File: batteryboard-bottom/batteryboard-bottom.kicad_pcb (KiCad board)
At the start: 2 copper layers, 46.8 x 46.8 mm, 7 parts, among them J1 Conn_01x10, J2 Conn_02x05_Odd_Even

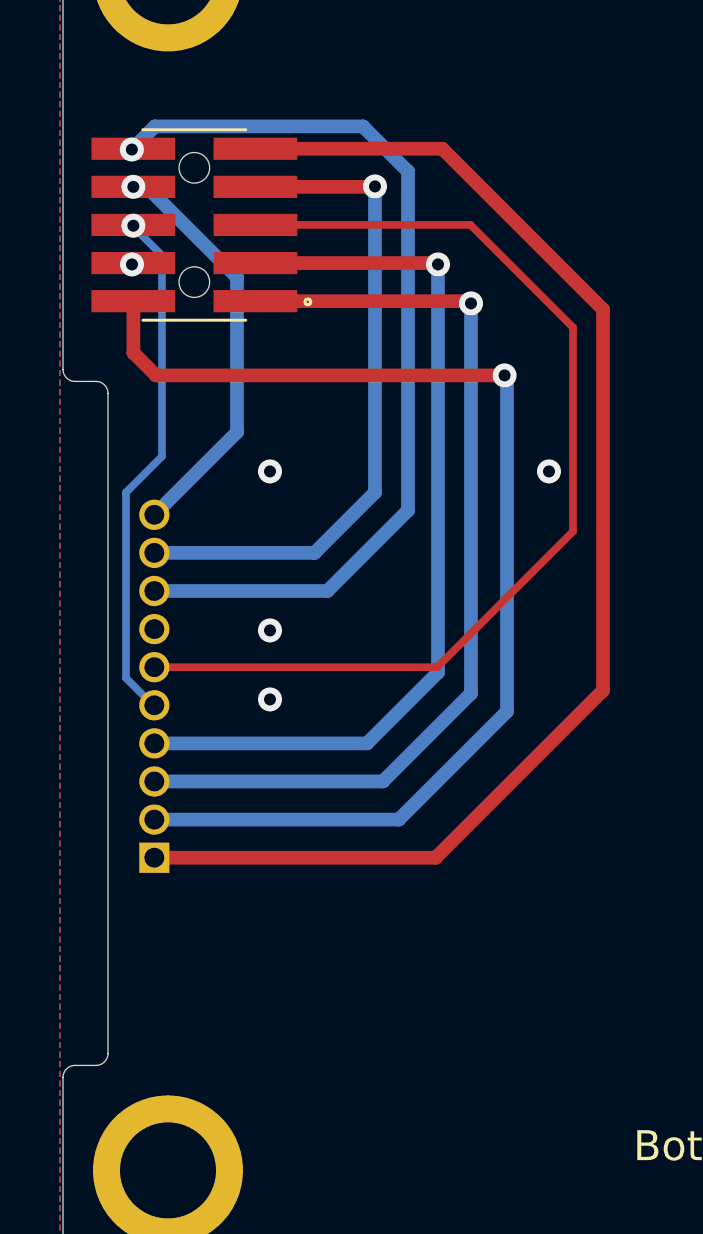
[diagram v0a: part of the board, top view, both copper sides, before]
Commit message: Updated connector position on bottom batteryboard
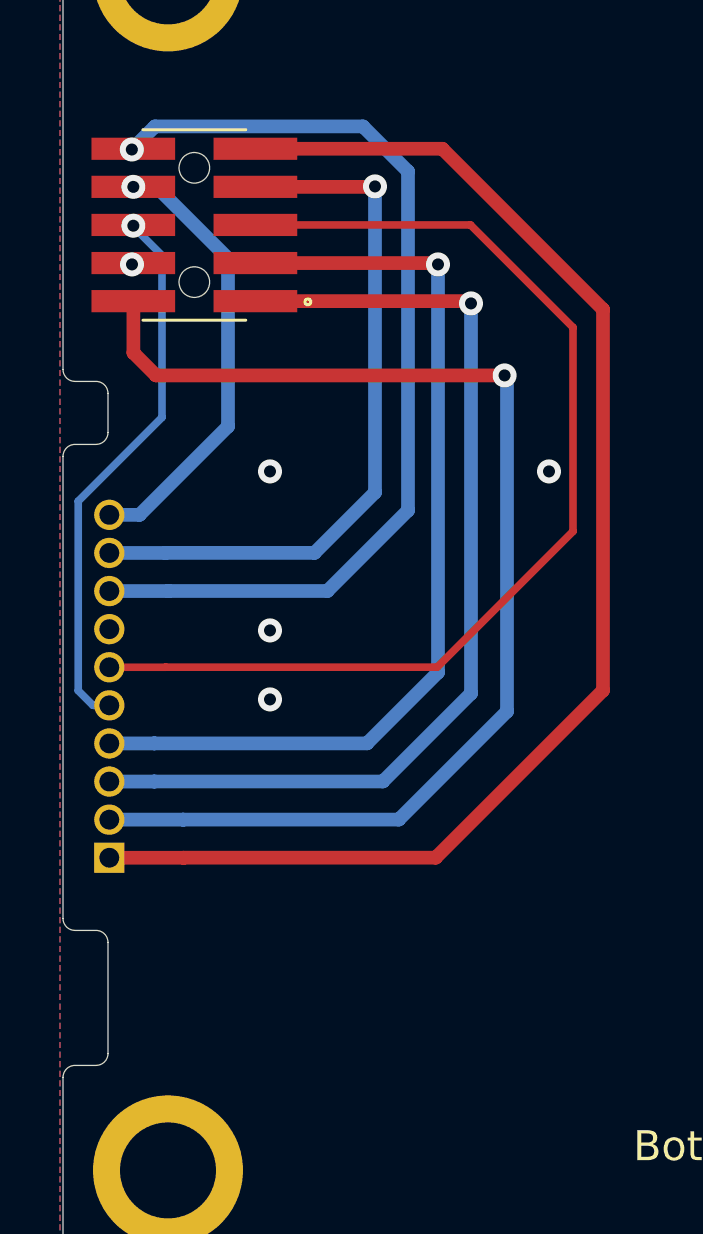
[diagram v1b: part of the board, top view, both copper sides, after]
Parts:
- moved J1 1.50 mm to (130.8, 105.5)
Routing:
- net VUSB: track 31.0 -> 32.5 mm
- net SDA3: track 34.6 -> 36.1 mm
- net BATT_P_SW: track 32.0 -> 33.5 mm
- net BATT_P: track 43.8 -> 45.3 mm
- net COIL5_P: track 22.4 -> 23.9 mm
- net BATT_N_SW: track 38.9 -> 40.4 mm
- net +3V3: track 30.1 -> 31.6 mm
- net COIL5_N: track 13.8 -> 14.9 mm
- net SCL3: track 17.3 -> 18.3 mm
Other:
- outline, holes or cut-outs redrawn
- board text added: "26-JUN-22"
- board text added: "v01.1"
- board text removed: "09-JUN-22"
- board text removed: "v01"

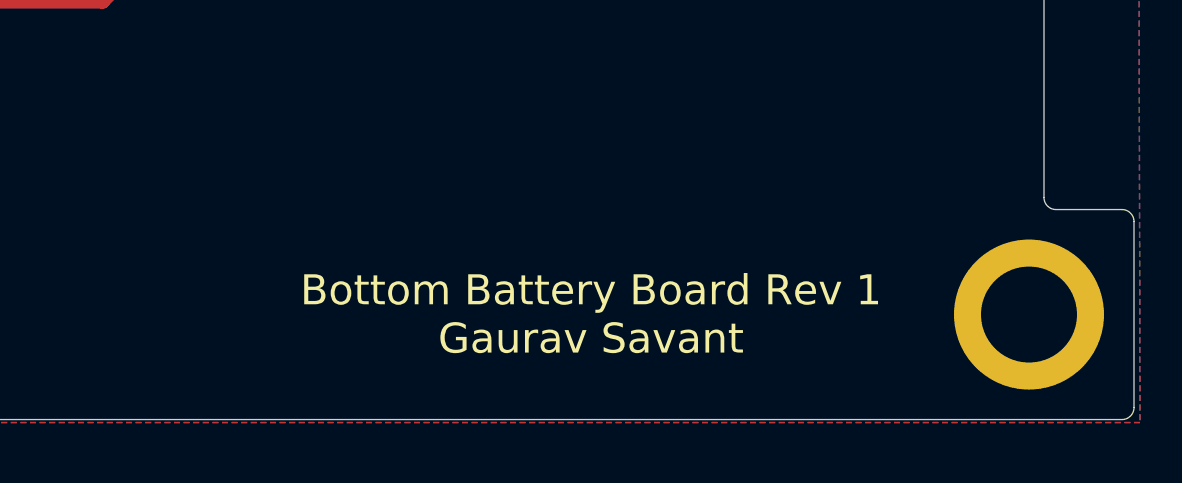
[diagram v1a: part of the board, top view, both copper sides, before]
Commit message: Updated connector position on top batteryboard
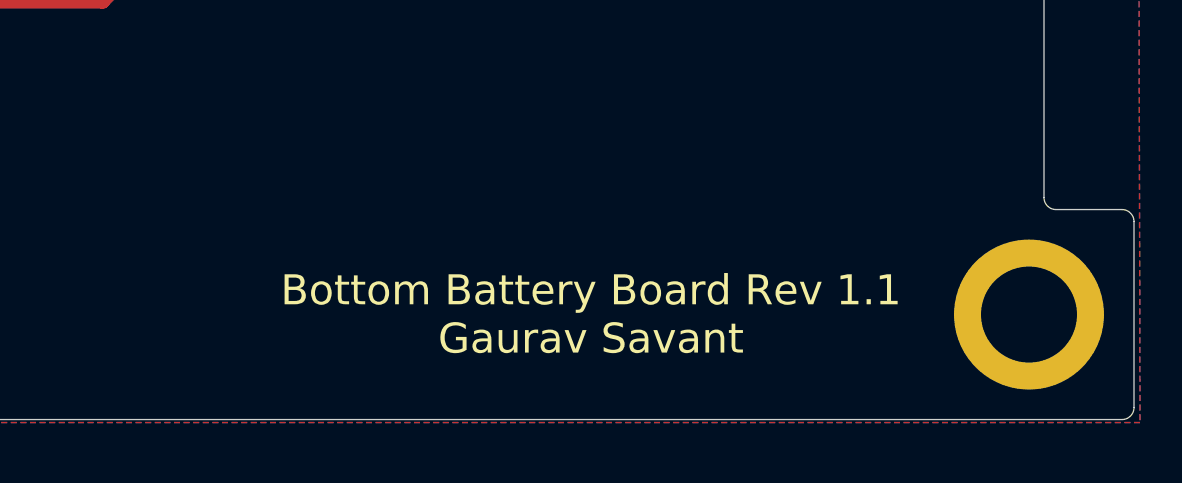
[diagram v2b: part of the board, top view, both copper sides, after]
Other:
- board text added: "Bottom Battery Board Rev 1.1 Gaurav Savant"
- board text removed: "Bottom Battery Board Rev 1 Gaurav Savant"
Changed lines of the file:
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@@
   (gr_line (start 175.699996 78.299998) (end 129.699995 78.299996) (layer "Edge.Cuts") (width 0.0254))
   (gr_line (start 175.7 118.100009) (end 173.5 118.099995) (layer "Edge.Cuts") (width 0.0254))
-  (gr_text "Bottom Battery Board Rev 1\nGaurav Savant\n" (at 158 121.6) (layer "F.SilkS")
+  (gr_text "Bottom Battery Board Rev 1.1\nGaurav Savant\n" (at 157.999989 121.600011) (layer "F.SilkS")
     (effects (font (size 1 1) (thickness 0.15)))
   )

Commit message: Recheck boards and re-export models
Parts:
- J1: value Conn_01x10 -> SLM-110-01-G-S
- J2: value Conn_02x05_Odd_Even -> FTS-105-01-L-DV-A
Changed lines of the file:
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@@
       (effects (font (size 1.27 1.27) (thickness 0.254)))
     )
-    (fp_text value "Conn_02x05_Odd_Even" (at 0 0 90) (layer "F.SilkS") hide
+    (fp_text value "FTS-105-01-L-DV-A" (at 0 0 90) (layer "F.SilkS") hide
       (effects (font (size 1.27 1.27) (thickness 0.254)))
     )
@@
   )
   (footprint "batteryboard:SAMTEC_TMS-110-01-G-S" (layer "B.Cu")
-    (at 130.844 105.463 90)
+    (at 130.844011 105.46301 90)
     (property "Sheetfile" "batteryboard-bottom.kicad_sch")
     (property "Sheetname" "")
@@
       (effects (font (size 1 1) (thickness 0.15)) (justify mirror))
     )
-    (fp_text value "Conn_01x10" (at 5.985 -2.849 270) (layer "B.Fab")
+    (fp_text value "SLM-110-01-G-S" (at 5.985 -2.849 270) (layer "B.Fab")
       (effects (font (size 1 1) (thickness 0.15)) (justify mirror))
     )
     (fp_line (start -6.35 -1.2192) (end -6.35 -0.855) (layer "B.SilkS") (width 0.2))
-    (fp_line (start -6.35 1.2192) (end -6.35 0.855) (layer "B.SilkS") (width 0.2))
-    (fp_line (start 6.35 -1.2192) (end 6.35 -0.855) (layer "B.SilkS") (width 0.2))
     (fp_line (start -6.35 -1.2192) (end 6.35 -1.2192) (layer "B.SilkS") (width 0.2))
     (fp_line (start -6.35 1.2192) (end 6.35 1.2192) (layer "B.SilkS") (width 0.2))
+    (fp_line (start -6.35 1.2192) (end -6.35 0.855) (layer "B.SilkS") (width 0.2))
     (fp_line (start 6.35 1.2192) (end 6.35 0.855) (layer "B.SilkS") (width 0.2))
+    (fp_line (start 6.35 -1.2192) (end 6.35 -0.855) (layer "B.SilkS") (width 0.2))
     (fp_circle (center -5.715 2.069) (end -5.615 2.069) (layer "B.SilkS") (width 0.2) (fill none))
+    (fp_line (start 6.6 -1.4692) (end 6.6 1.4692) (layer "B.CrtYd") (width 0.05))
     (fp_line (start -6.6 -1.4692) (end 6.6 -1.4692) (layer "B.CrtYd") (width 0.05))
     (fp_line (start -6.6 -1.4692) (end -6.6 1.4692) (layer "B.CrtYd") (width 0.05))
     (fp_line (start -6.6 1.4692) (end 6.6 1.4692) (layer "B.CrtYd") (width 0.05))
-    (fp_line (start 6.6 -1.4692) (end 6.6 1.4692) (layer "B.CrtYd") (width 0.05))
+    (fp_line (start -6.35 1.2192) (end 6.35 1.2192) (layer "B.Fab") (width 0.1))
     (fp_line (start 6.35 -1.2192) (end 6.35 1.2192) (layer "B.Fab") (width 0.1))
+    (fp_line (start -6.35 -1.2192) (end -6.35 1.2192) (layer "B.Fab") (width 0.1))
     (fp_line (start -6.35 -1.2192) (end 6.35 -1.2192) (layer "B.Fab") (width 0.1))
-    (fp_line (start -6.35 -1.2192) (end -6.35 1.2192) (layer "B.Fab") (width 0.1))
-    (fp_line (start -6.35 1.2192) (end 6.35 1.2192) (layer "B.Fab") (width 0.1))
     (fp_circle (center -5.715 2.069) (end -5.615 2.069) (layer "B.Fab") (width 0.2) (fill none))
-    (pad "01" thru_hole rect (at -5.715 0 90) (size 1.01 1.01) (drill 0.66) (layers *.Cu *.Mask)
+    (pad "1" thru_hole rect (at -5.715 0 90) (size 1.01 1.01) (drill 0.66) (layers *.Cu *.Mask)
       (net 7 "BATT_P") (pinfunction "Pin_1") (pintype "passive"))
-    (pad "02" thru_hole circle (at -4.445 0 90) (size 1.01 1.01) (drill 0.66) (layers *.Cu *.Mask)
+    (pad "2" thru_hole circle (at -4.445 0 90) (size 1.01 1.01) (drill 0.66) (layers *.Cu *.Mask)
       (net 2 "BATT_N_SW") (pinfunction "Pin_2") (pintype "passive"))
-    (pad "03" thru_hole circle (at -3.175 0 90) (size 1.01 1.01) (drill 0.66) (layers *.Cu *.Mask)
+    (pad "3" thru_hole circle (at -3.175 0 90) (size 1.01 1.01) (drill 0.66) (layers *.Cu *.Mask)
       (net 1 "BATT_P_SW") (pinfunction "Pin_3") (pintype "passive"))
-    (pad "04" thru_hole circle (at -1.905 0 90) (size 1.01 1.01) (drill 0.66) (layers *.Cu *.Mask)
+    (pad "4" thru_hole circle (at -1.905 0 90) (size 1.01 1.01) (drill 0.66) (layers *.Cu *.Mask)
       (net 4 "+3V3") (pinfunction "Pin_4") (pintype "passive"))
-    (pad "05" thru_hole circle (at -0.635 0 90) (size 1.01 1.01) (drill 0.66) (layers *.Cu *.Mask)
+    (pad "5" thru_hole circle (at -0.635 0 90) (size 1.01 1.01) (drill 0.66) (layers *.Cu *.Mask)
       (net 6 "SCL3") (pinfunction "Pin_5") (pintype "passive"))
-    (pad "06" thru_hole circle (at 0.635 0 90) (size 1.01 1.01) (drill 0.66) (layers *.Cu *.Mask)
+    (pad "6" thru_hole circle (at 0.635 0 90) (size 1.01 1.01) (drill 0.66) (layers *.Cu *.Mask)
       (net 5 "SDA3") (pinfunction "Pin_6") (pintype "passive"))
-    (pad "07" thru_hole circle (at 1.905 0 90) (size 1.01 1.01) (drill 0.66) (layers *.Cu *.Mask)
+    (pad "7" thru_hole circle (at 1.905 0 90) (size 1.01 1.01) (drill 0.66) (layers *.Cu *.Mask)
       (net 3 "GND") (pinfunction "Pin_7") (pintype "passive"))
-    (pad "08" thru_hole circle (at 3.175 0 90) (size 1.01 1.01) (drill 0.66) (layers *.Cu *.Mask)
+    (pad "8" thru_hole circle (at 3.175 0 90) (size 1.01 1.01) (drill 0.66) (layers *.Cu *.Mask)
       (net 10 "VUSB") (pinfunction "Pin_8") (pintype "passive"))
-    (pad "09" thru_hole circle (at 4.445 0 90) (size 1.01 1.01) (drill 0.66) (layers *.Cu *.Mask)
+    (pad "9" thru_hole circle (at 4.445 0 90) (size 1.01 1.01) (drill 0.66) (layers *.Cu *.Mask)
       (net 9 "COIL5_P") (pinfunction "Pin_9") (pintype "passive"))
     (pad "10" thru_hole circle (at 5.715 0 90) (size 1.01 1.01) (drill 0.66) (layers *.Cu *.Mask)
       (net 8 "COIL5_N") (pinfunction "Pin_10") (pintype "passive"))
-    (model "C:/Users/Neil/Desktop/avionics-batteryboard/kicad-libs/3d/TMS-110-01-G-S.step"
+    (model "${KIPRJMOD}/../kicad-libs/3d/TMS-110-01-G-S.step" hide
       (offset (xyz 0 0 0))
       (scale (xyz 1 1 1))
+      (rotate (xyz -90 0 0))
+    )
+    (model "${KIPRJMOD}/../kicad-libs/3d/SLM-110-01-G-S.stp"
+      (offset (xyz 0 0 0))
+      (scale (xyz 1 1 1))

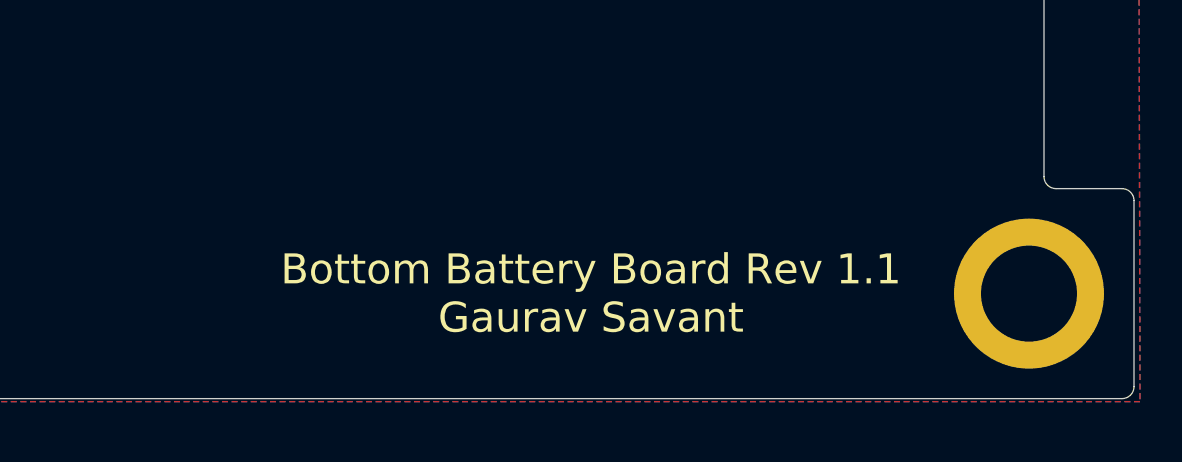
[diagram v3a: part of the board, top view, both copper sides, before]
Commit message: modified/standardized silkscreen
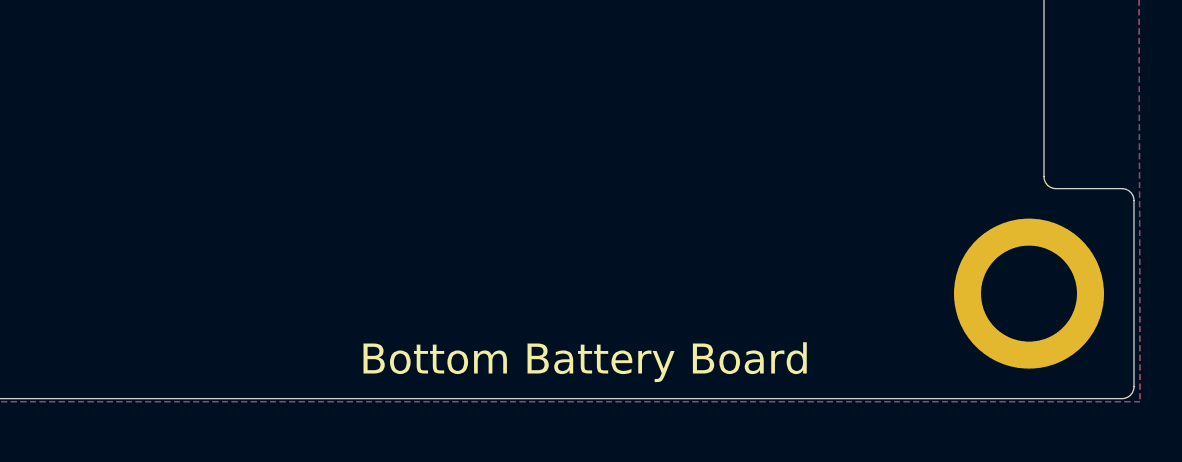
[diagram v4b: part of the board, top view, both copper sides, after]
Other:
- board text added: "Bottom Battery Board"
- board text removed: "Bottom Battery Board Rev 1.1 Gaurav Savant"
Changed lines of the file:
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@@
   (gr_line (start 175.699996 78.299998) (end 129.699995 78.299996) (layer "Edge.Cuts") (width 0.0254))
   (gr_line (start 175.7 118.100009) (end 173.5 118.099995) (layer "Edge.Cuts") (width 0.0254))
-  (gr_text "Bottom Battery Board Rev 1.1\nGaurav Savant\n" (at 157.999989 121.600011) (layer "F.SilkS")
+  (gr_text "Bottom Battery Board" (at 157.8 123.8) (layer "F.SilkS")
     (effects (font (size 1 1) (thickness 0.15)))
   )

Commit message: Export New Gerbers
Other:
- board text added: "06-JUL-22"
- board text removed: "26-JUN-22"
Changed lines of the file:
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@@
       (outputformat 1)
       (mirror false)
-      (drillshape 1)
+      (drillshape 0)
       (scaleselection 1)
-      (outputdirectory "")
+      (outputdirectory "../gerbers/batteryboard-bottom (07-06-22)/")
     )
   )
@@
   (gr_line (start 175.699996 78.299998) (end 129.699995 78.299996) (layer "Edge.Cuts") (width 0.0254))
   (gr_line (start 175.7 118.100009) (end 173.5 118.099995) (layer "Edge.Cuts") (width 0.0254))
-  (gr_text "Bottom Battery Board" (at 157.8 123.8) (layer "F.SilkS")
-    (effects (font (size 1 1) (thickness 0.15)))
+  (gr_text "Bottom Battery Board" (at 171.425 101.7 90) (layer "F.SilkS")
+    (effects (font (size 0.889 0.889) (thickness 0.127)))
   )
-  (gr_text "26-JUN-22" (at 154.1668 80.8952) (layer "F.Mask")
+  (gr_text "06-JUL-22" (at 154.166799 80.89519) (layer "F.Mask")
     (effects (font (size 0.635 0.635) (thickness 0.1524)) (justify right))
   )

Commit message: B1/03 updates
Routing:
- net SDA3: track 36.1 -> 16.7 mm, vias 0 -> 1
- net BATT_N_SW: track 40.4 -> 21.0 mm, vias 1 -> 0
- net VUSB: track 32.5 -> 16.8 mm
- net +3V3: track 31.6 -> 18.8 mm
- net BATT_P: track 45.3 -> 35.5 mm
- net BATT_P_SW: track 33.5 -> 24.7 mm, vias 1 -> 3
- net SCL3: track 18.3 -> 23.7 mm
- net COIL5_N: track 14.9 -> 11.9 mm
- net COIL5_P: track 23.9 -> 22.6 mm
- net GND: vias 5 -> 2
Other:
- board text added: "06-SEP-22"
- board text added: "Rev B1/03"
- board text removed: "06-JUL-22"
- board text removed: "v01.1"

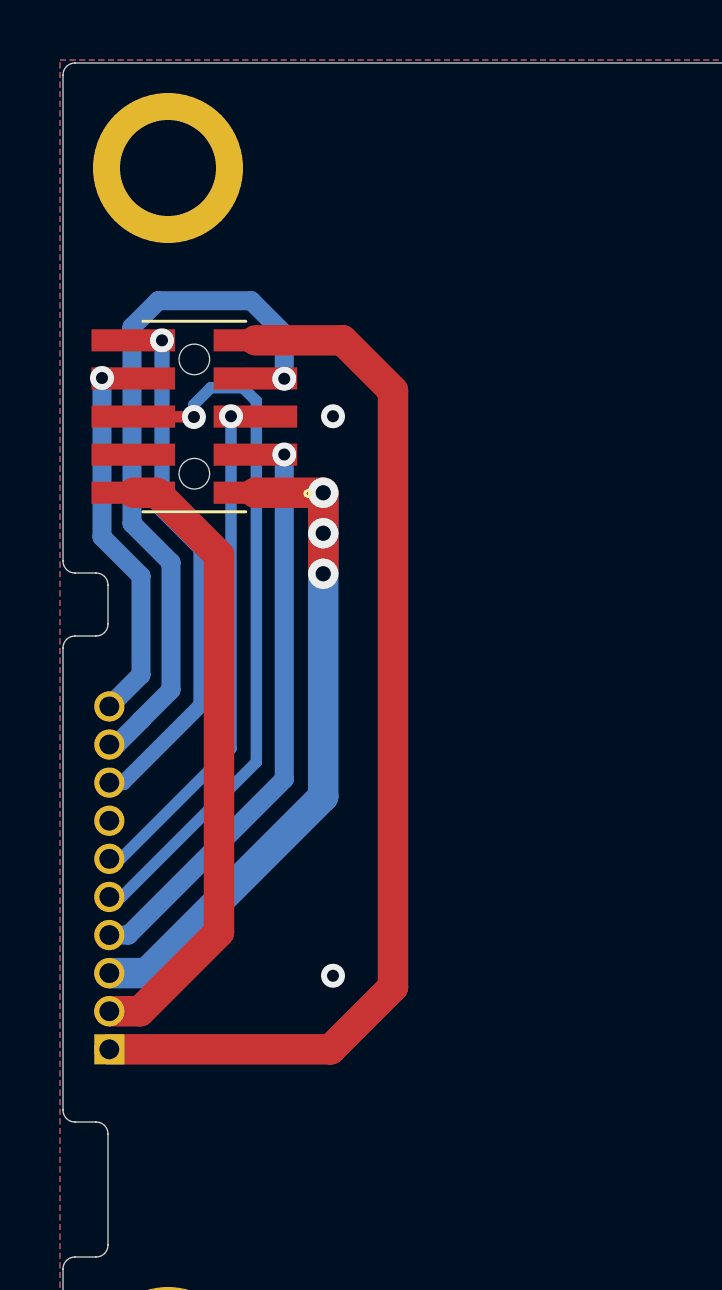
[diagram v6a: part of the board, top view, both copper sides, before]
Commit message: Widened Power Traces, Added Notch for Antenna Cable Routing
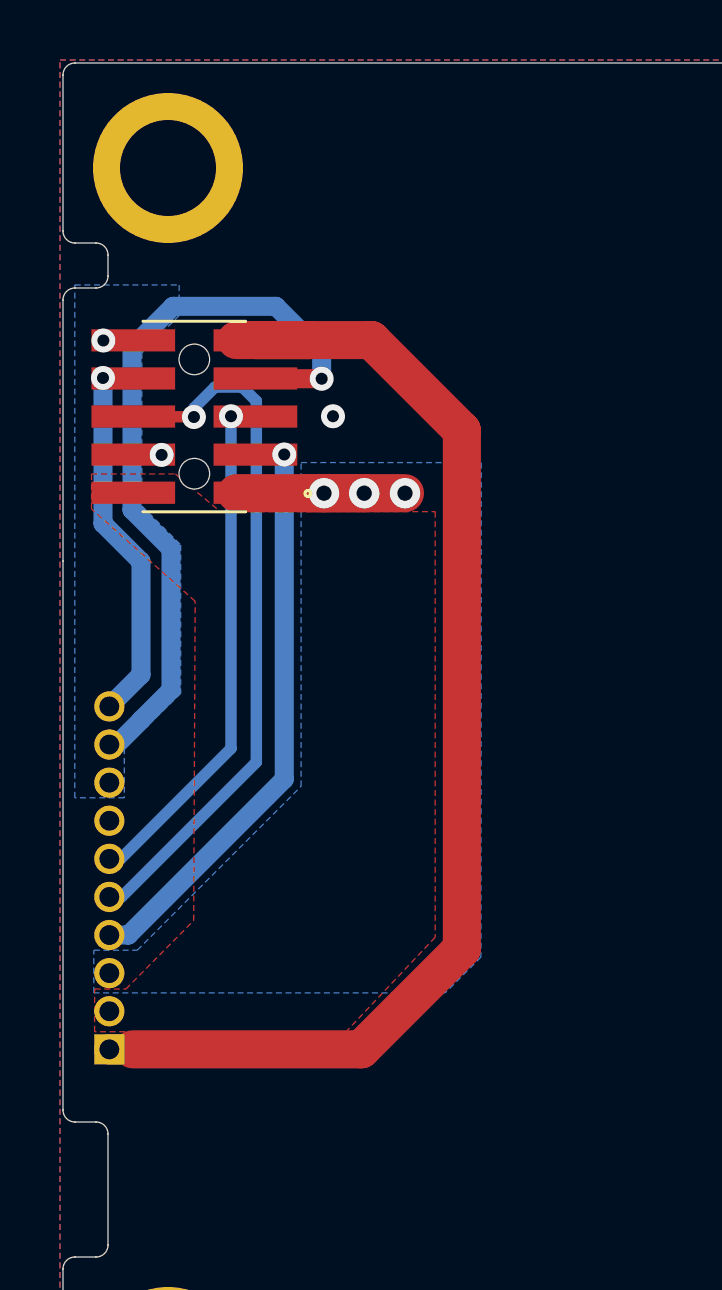
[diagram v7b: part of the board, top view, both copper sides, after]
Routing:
- net BATT_N_SW: track 21.0 -> 0.00 mm
- net BATT_P_SW: track 24.7 -> 7.51 mm
- net VUSB: track 16.8 -> 0.42 mm
- net BATT_P: track 35.5 -> 40.9 mm
- net COIL5_P: track 22.6 -> 25.2 mm
- added copper zone on F.Cu, net BATT_N_SW
- added copper zone on B.Cu, net BATT_P_SW
- added copper zone on B.Cu, net VUSB
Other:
- outline, holes or cut-outs redrawn
